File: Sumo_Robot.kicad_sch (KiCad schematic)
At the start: 0 parts

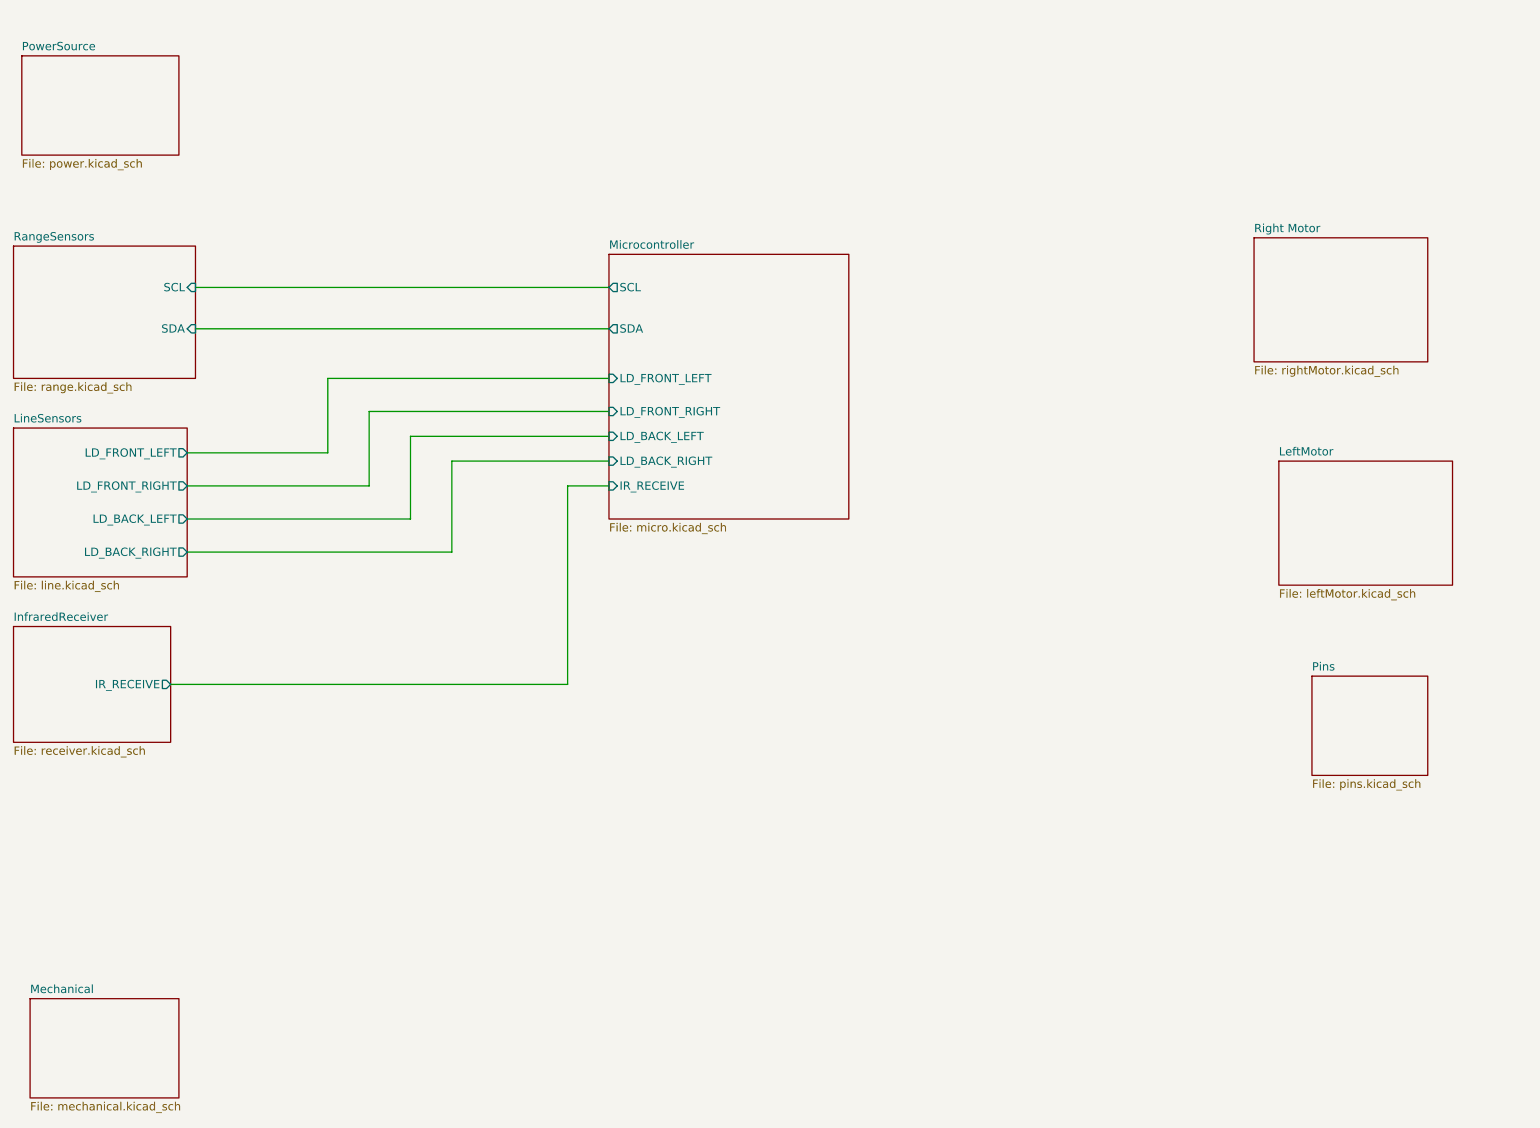
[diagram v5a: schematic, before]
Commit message: started adding DC Motor controller logic
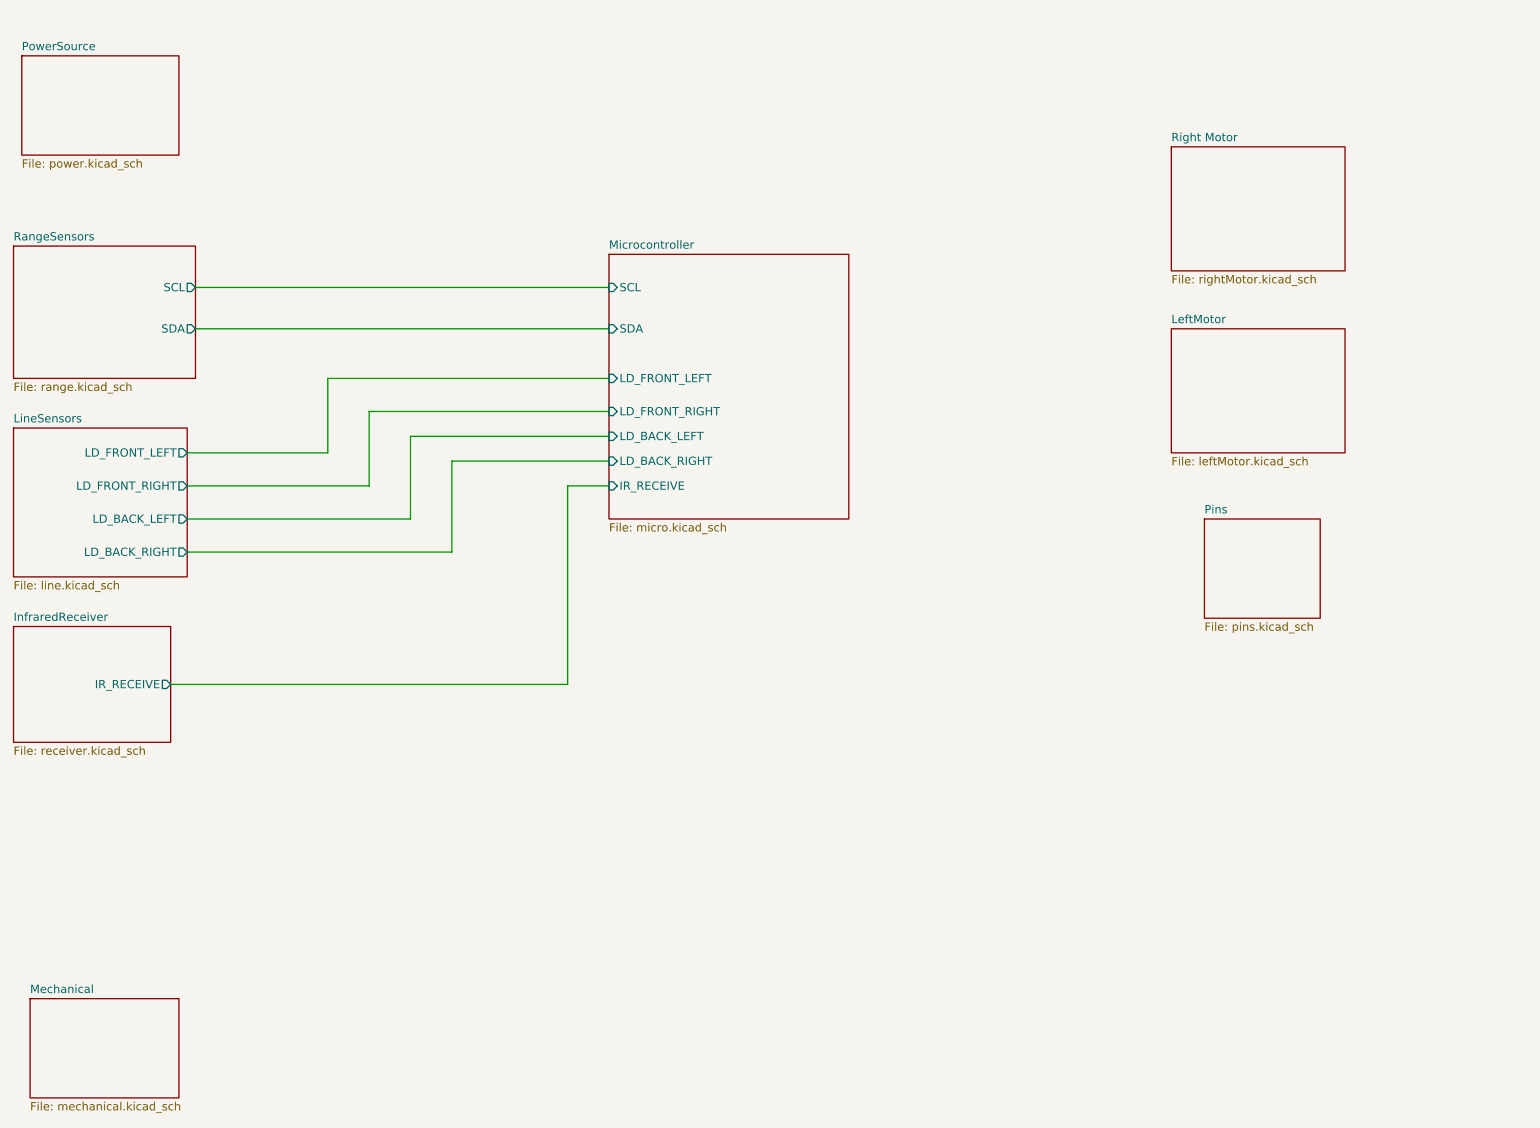
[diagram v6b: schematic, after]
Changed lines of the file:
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@@
 	)
 	(sheet
-		(at 232.41 127)
+		(at 215.9 102.87)
 		(size 17.78 15.24)
 		(exclude_from_sim no)
@@
 		)
 		(property "Sheetname" "Pins"
-			(at 232.41 126.2884 0)
+			(at 215.9 102.1584 0)
 			(effects
 				(font
@@
 		)
 		(property "Sheetfile" "pins.kicad_sch"
-			(at 232.41 142.8246 0)
+			(at 215.9 118.6946 0)
 			(effects
 				(font
@@
 			)
 		)
-		(pin "SCL" output
-			(at 124.46 67.31 180)
-			(effects
-				(font
-					(size 1.27 1.27)
-				)
-				(justify left)
-			)
-		)
-		(pin "SDA" output
-			(at 124.46 73.66 180)
-			(effects
-				(font
-					(size 1.27 1.27)
-				)
-				(justify left)
-			)
-		)
 		(pin "IR_RECEIVE" input
 			(at 124.46 97.79 180)
@@
 			)
 		)
+		(pin "SDA" input
+			(at 124.46 73.66 180)
+			(effects
+				(font
+					(size 1.27 1.27)
+				)
+				(justify left)
+			)
+		)
+		(pin "SCL" input
+			(at 124.46 67.31 180)
+			(effects
+				(font
+					(size 1.27 1.27)
+				)
+				(justify left)
+			)
+		)
 		(instances
 			(project "Sumo_Robot"
@@
 	)
 	(sheet
-		(at 227.33 93.98)
+		(at 210.82 73.66)
 		(size 26.67 19.05)
 		(exclude_from_sim no)
@@
 		)
 		(property "Sheetname" "LeftMotor"
-			(at 227.33 93.2684 0)
+			(at 210.82 72.9484 0)
 			(effects
 				(font
@@
 		)
 		(property "Sheetfile" "leftMotor.kicad_sch"
-			(at 227.33 113.6146 0)
+			(at 210.82 93.2946 0)
 			(effects
 				(font
@@
 			)
 		)
-		(pin "SCL" input
+		(pin "SCL" output
 			(at 60.96 67.31 0)
 			(effects
@@
 			)
 		)
-		(pin "SDA" input
+		(pin "SDA" output
 			(at 60.96 73.66 0)
 			(effects
@@
 	)
 	(sheet
-		(at 223.52 59.69)
+		(at 210.82 45.72)
 		(size 26.67 19.05)
 		(exclude_from_sim no)
@@
 		)
 		(property "Sheetname" "Right Motor"
-			(at 223.52 58.9784 0)
+			(at 210.82 45.0084 0)
 			(effects
 				(font
@@
 		)
 		(property "Sheetfile" "rightMotor.kicad_sch"
-			(at 223.52 79.3246 0)
-			(effects
-				(font
+			(at 210.82 65.3546 0)
+			(effects
+				(font

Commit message: added motor functionality to the MCU
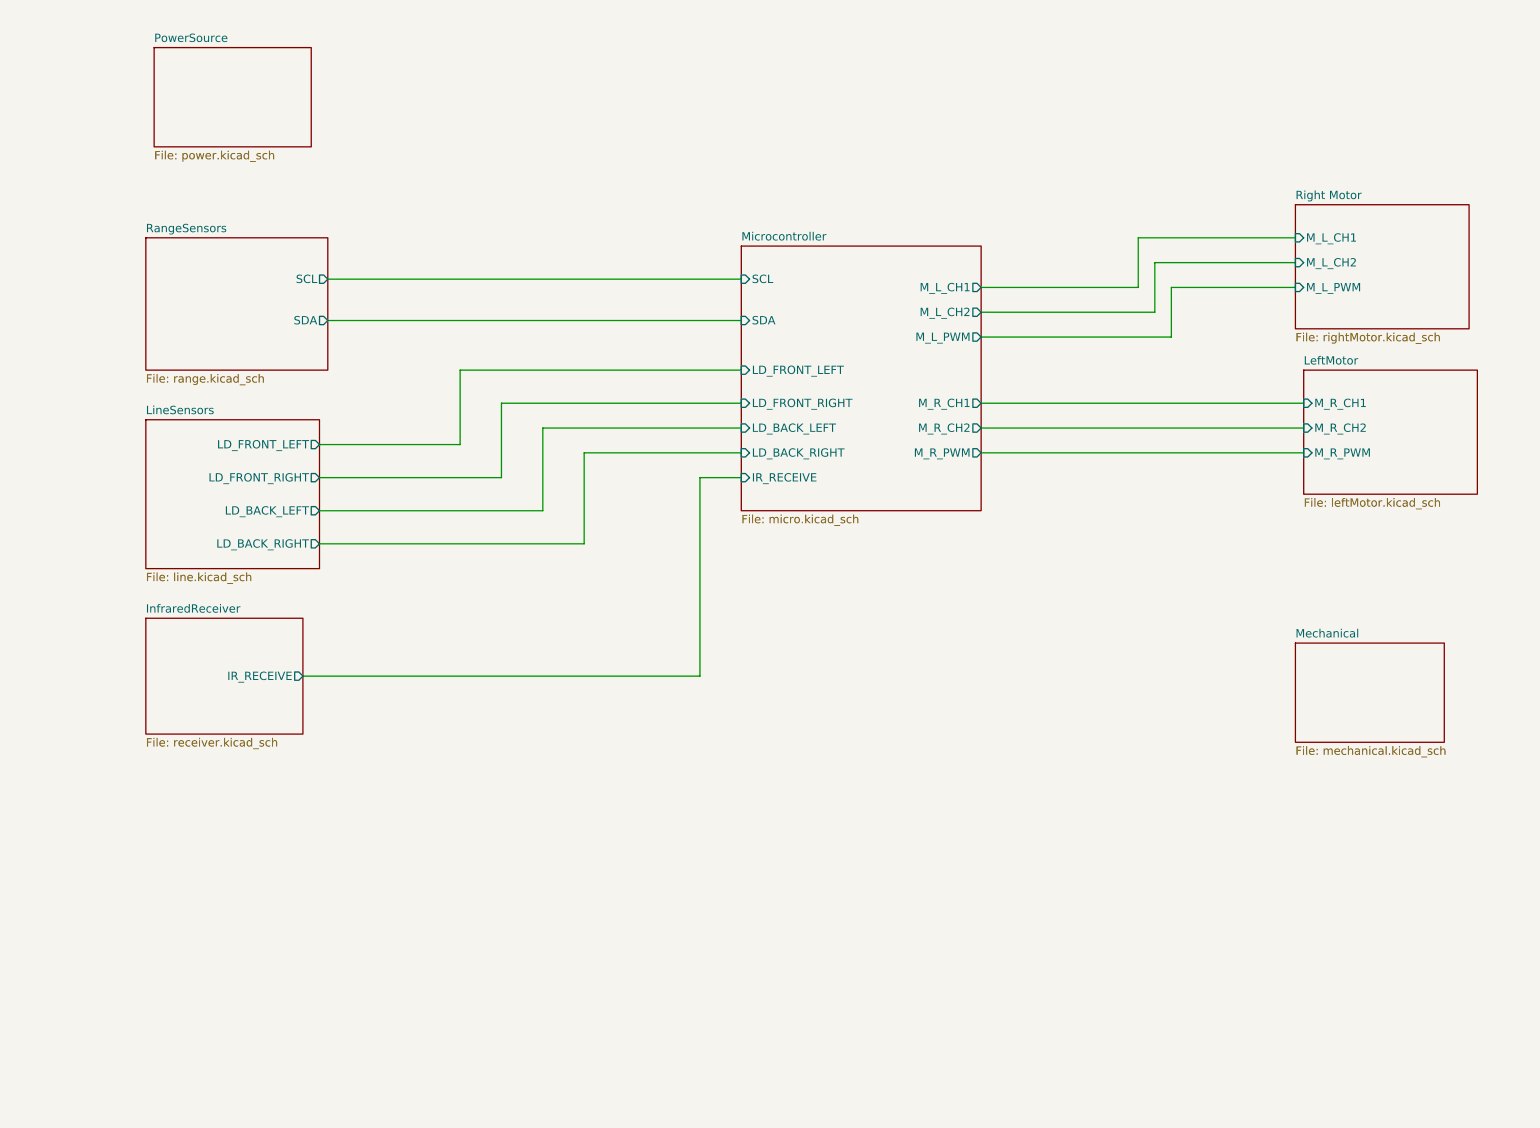
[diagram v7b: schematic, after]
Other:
- removed sheet Pins
- sheet LeftMotor ports: added M_R_CH1, M_R_CH2, M_R_PWM; removed none
- sheet Microcontroller ports: added M_L_CH1, M_L_CH2, M_L_PWM, M_R_CH1, M_R_CH2, M_R_PWM; removed none
- sheet Right Motor ports: added M_L_CH1, M_L_CH2, M_L_PWM; removed none

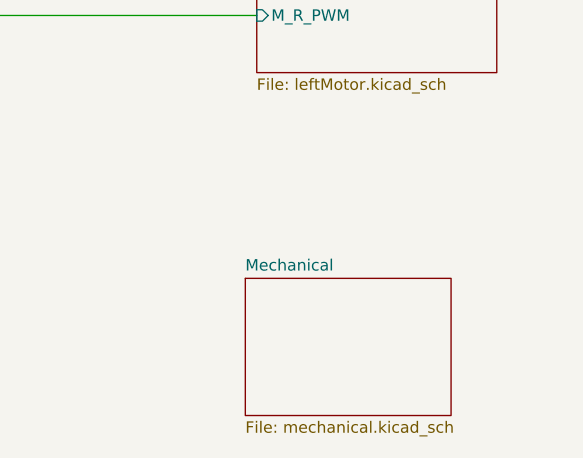
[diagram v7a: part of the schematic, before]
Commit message: updated MCU schematic
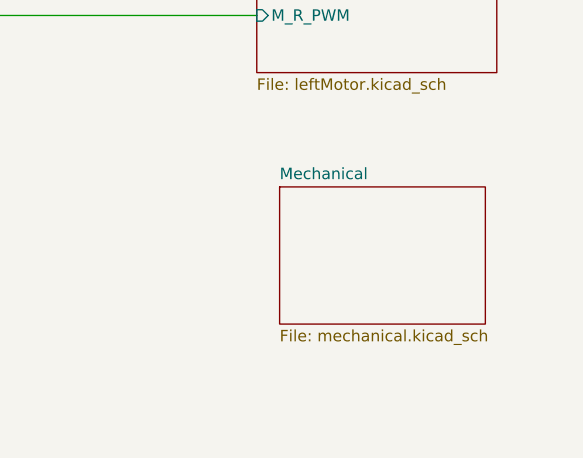
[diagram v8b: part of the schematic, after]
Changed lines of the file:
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@@
 	)
 	(sheet
-		(at 229.87 121.92)
+		(at 233.68 111.76)
 		(size 22.86 15.24)
 		(exclude_from_sim no)
@@
 		)
 		(property "Sheetname" "Mechanical"
-			(at 229.87 121.2084 0)
+			(at 233.68 111.0484 0)
 			(effects
 				(font
@@
 		)
 		(property "Sheetfile" "mechanical.kicad_sch"
-			(at 229.87 137.7446 0)
+			(at 233.68 127.5846 0)
 			(effects
 				(font
